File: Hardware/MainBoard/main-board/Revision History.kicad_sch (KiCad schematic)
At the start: 0 parts

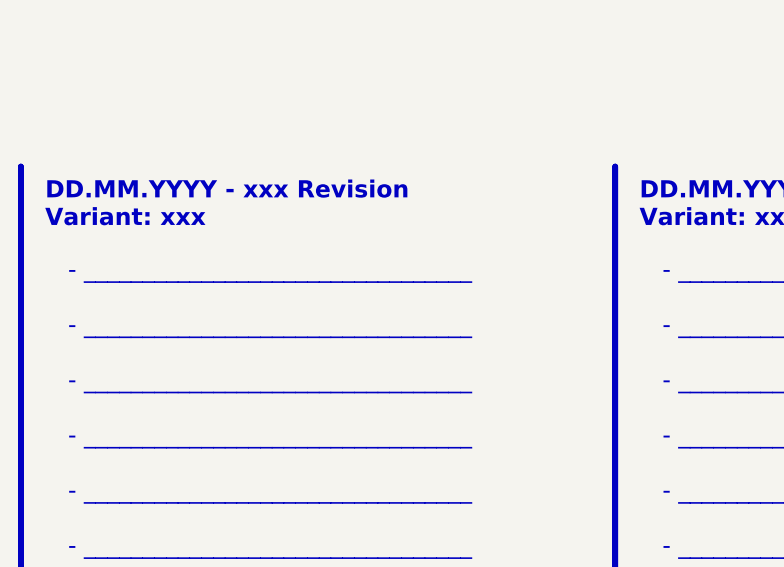
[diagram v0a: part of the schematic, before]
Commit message: add details, need to change TC amp gain for different voltage and temperature
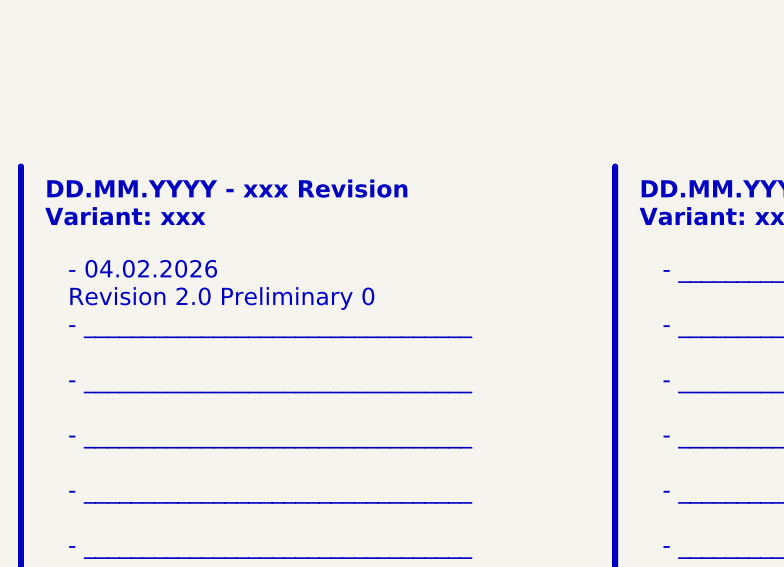
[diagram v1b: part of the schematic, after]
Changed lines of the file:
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@@
 		)
 	)
-	(text_box "- _________________________________\n\n- _________________________________\n\n- _________________________________\n\n- _________________________________\n\n- _________________________________\n\n- _________________________________\n\n- _________________________________\n\n- _________________________________\n\n- _________________________________\n\n- _________________________________\n\n- _________________________________\n\n- _________________________________\n\n- _________________________________\n\n- _________________________________\n\n- _________________________________\n\n- _________________________________\n\n- _________________________________"
+	(text_box "- 04.02.2026\n   Revision 2.0 Preliminary 0\n- _________________________________\n\n- _________________________________\n\n- _________________________________\n\n- _________________________________\n\n- _________________________________\n\n- _________________________________\n\n- _________________________________\n\n- _________________________________\n\n- _________________________________\n\n- _________________________________\n\n- _________________________________\n\n- _________________________________\n\n- _________________________________\n\n- _________________________________\n\n- _________________________________\n\n- _________________________________"
 		(exclude_from_sim no)
 		(at 24.13 45.72 0)
@@
 		(stroke
 			(width -0.0001)
-			(type default)
+			(type solid)
 		)
 		(fill
